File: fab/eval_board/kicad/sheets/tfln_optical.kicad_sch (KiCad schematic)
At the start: 5 parts, among them J11 MPO-24, U21 AD7928, U24 AD5684R, U25 TMP461, U3 TFLN_PIC

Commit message: fix: regenerate KiCad files in valid KiCad 8 format
- Rewrote all .kicad_sch files with proper lib_symbols sections,
  symbol instances, wires, hierarchical sheet references, and
  power port definitions (removed invalid ';;' comment syntax)
- Fixed .kicad_pcb: removed comment lines, added 922 missing net
  definitions, fixed gr_text justify format
- Regenerated Gerbers from fixed PCB using kicad-cli (30 files)
- All files validated with kicad-cli: schematic exports 5-page PDF,
  PCB exports SVG, DRC/ERC both run without parse errors
- Added regenerate_kicad.py generator script for reproducibility

Co-Authored-By: Bola Olatunji <bola.olatunji@ai.lightos.sh>
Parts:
- removed J11: MPO-24, LightRail:MPO-24, symbol Connector:MPO-24
- added J10, J7, J8, J9: SMA_RF_Probe, Connector_Coaxial:SMA_Amphenol_132134-11_Vertical, symbol Connector:SMA
- added J11: MPO-24, LightRail:MPO-24, symbol Connector_Fiber:MPO_24
- U21: value AD7928 -> AD7928BRUZ
- U24: value AD5684R -> AD5684RBRUZ
- U25: value TMP461 -> TMP461AIDR; footprint Package_SON:WSON-8-1EP_2x2mm_P0.5mm -> Package_SO:SOIC-8_3.9x4.9mm_P1.27mm
- U3: value TFLN_PIC -> TFLN_Optical_Module; MPN LR-TFLN-PIC-001 -> (none)
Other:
- note removed: "AC Coupling — TFLN TX Drive: C10_1 through C10_16: 100nF 0201 (GRM033R71A104KA01D) Placed within 1mm of TFLN RF input pads 100Ω differential impedance maintained through coupling"
- note removed: "OPTICAL KEEP-OUT ZONE: 40mm x 15mm centered on TFLN PIC No copper pour, no vias, no traces within ±50µm alignment tolerance Edge-coupler fiber interface at top edge"
- title: TFLN Optical Engine + Monitor/Bias — LightRail Eval Board -> TFLN Optical Engine - LightRail Eval Board

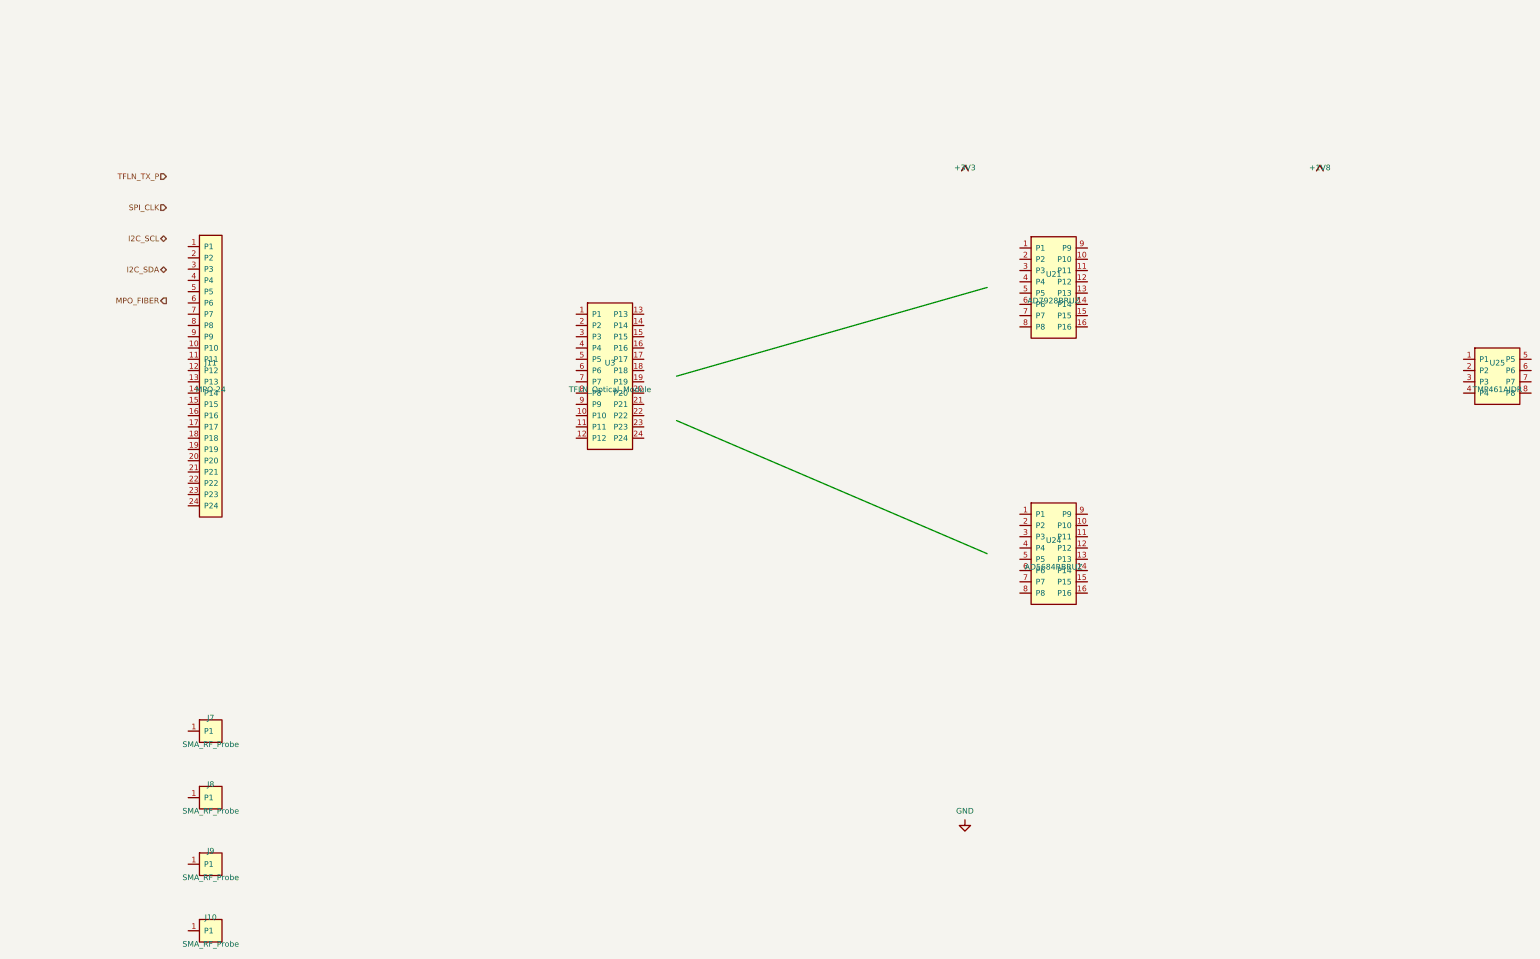
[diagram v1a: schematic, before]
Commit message: refactor: improve ERC quality via grid snapping and power flags
Co-Authored-By: Bola Olatunji <bola.olatunji@ai.lightos.sh>
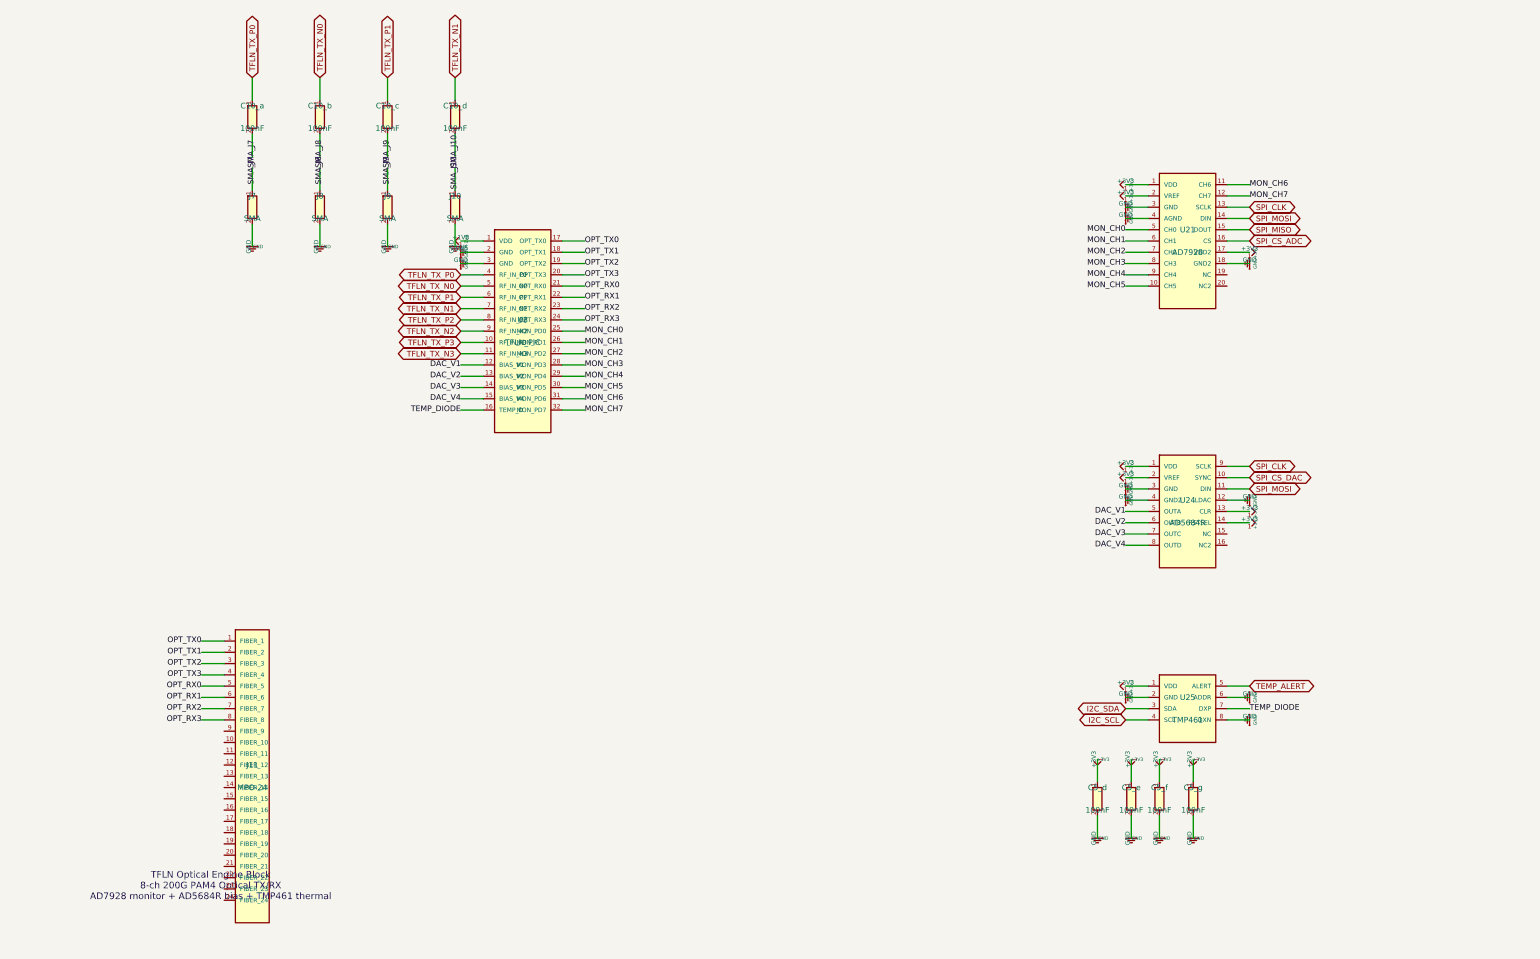
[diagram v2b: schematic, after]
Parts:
- added C10_a, C10_b, C10_c, C10_d, C5_d, C5_e, C5_f, C5_g: 100nF, symbol Device:C
- J10, J7, J8, J9: value SMA_RF_Probe -> SMA; footprint Connector_Coaxial:SMA_Amphenol_132134-11_Vertical -> Connector_Coaxial:SMA_Edge
- J11: footprint LightRail:MPO-24 -> Connector:MPO_24_SMT
- U21: value AD7928BRUZ -> AD7928; footprint Package_SO:TSSOP-20_4.4x6.5mm_P0.65mm -> Package_SO:TSSOP-20
- U24: value AD5684RBRUZ -> AD5684R; footprint Package_SO:TSSOP-16_4.4x5mm_P0.65mm -> Package_SO:TSSOP-16
- U25: value TMP461AIDR -> TMP461; footprint Package_SO:SOIC-8_3.9x4.9mm_P1.27mm -> Package_SON:WSON-8_2x2mm
- U3: value TFLN_Optical_Module -> TFLN_PIC; footprint LightRail:Custom_Optical_Module -> LightRail:TFLN_PIC_Module; MPN (none) -> LR-TFLN-PIC-001
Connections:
- net +1V8: now also U3.1 (VDD)
- net +3V3: now also U21.1 (VDD), U21.17 (VDD2), U21.2 (VREF), U24.1 (VDD), U24.13 (CLR), U24.14 (RSTSEL), U24.2 (VREF), U25.1 (VDD), C5_d.1, C5_e.1, C5_f.1, C5_g.1
- net GND: now also J10.2, J7.2, J8.2, J9.2, U21.18 (GND2), U21.3 (GND), U21.4 (AGND), U24.12 (LDAC), U24.3 (GND), U24.4 (GND2), U25.2 (GND), U25.6 (ADDR), U25.8 (DXN), U3.2 (GND), U3.3 (GND), C5_d.2, C5_e.2, C5_f.2, C5_g.2
- net I2C_SCL: now also U25.4 (SCL)
- net I2C_SDA: now also U25.3 (SDA)
- net SPI_CLK: now also U21.13 (SCLK), U24.9 (SCLK)
- net SMA_J10: now reaches J10.1
- net SMA_J10: now also C10_d.2
- net SMA_J8: now reaches J8.1
- net SMA_J8: now also C10_b.2
- net OPT_TX0: now reaches J11.1 (FIBER_1)
- net OPT_TX0: now also U3.17 (OPT_TX0)
- net OPT_TX1: now reaches J11.2 (FIBER_2)
- net OPT_TX1: now also U3.18 (OPT_TX1)
- net OPT_TX2: now reaches J11.3 (FIBER_3)
- net OPT_TX2: now also U3.19 (OPT_TX2)
- net OPT_TX3: now reaches J11.4 (FIBER_4)
- net OPT_TX3: now also U3.20 (OPT_TX3)
- net OPT_RX0: now reaches J11.5 (FIBER_5)
- net OPT_RX0: now also U3.21 (OPT_RX0)
- net OPT_RX1: now reaches J11.6 (FIBER_6)
- net OPT_RX1: now also U3.22 (OPT_RX1)
- net OPT_RX2: now reaches J11.7 (FIBER_7)
- net OPT_RX2: now also U3.23 (OPT_RX2)
- net OPT_RX3: now reaches J11.8 (FIBER_8)
- net OPT_RX3: now also U3.24 (OPT_RX3)
- net MON_CH5: now reaches U21.10 (CH5)
- net MON_CH5: now also U3.30 (MON_PD5)
- net MON_CH6: now reaches U21.11 (CH6)
- net MON_CH6: now also U3.31 (MON_PD6)
- net MON_CH7: now reaches U21.12 (CH7)
- net MON_CH7: now also U3.32 (MON_PD7)
- net SPI_MOSI: now reaches U21.14 (DIN)
- net SPI_MOSI: now also U24.11 (DIN)
- net SPI_MISO: now reaches U21.15 (DOUT)
- net SPI_CS_ADC: now reaches U21.16 (CS)
- net MON_CH0: now reaches U21.5 (CH0)
- net MON_CH0: now also U3.25 (MON_PD0)
- net MON_CH1: now reaches U21.6 (CH1)
- net MON_CH1: now also U3.26 (MON_PD1)
- net MON_CH2: now reaches U21.7 (CH2)
- net MON_CH2: now also U3.27 (MON_PD2)
- net MON_CH3: now reaches U21.8 (CH3)
- net MON_CH3: now also U3.28 (MON_PD3)
- net MON_CH4: now reaches U21.9 (CH4)
- net MON_CH4: now also U3.29 (MON_PD4)
- net TEMP_ALERT: now reaches U25.5 (ALERT)
- net TEMP_DIODE: now reaches U25.7 (DXP)
- net TEMP_DIODE: now also U3.16 (TEMP_D)
- net SPI_CS_DAC: now reaches U24.10 (SYNC)
- net DAC_V1: now reaches U24.5 (OUTA)
- net DAC_V1: now also U3.12 (BIAS_V1)
- net DAC_V2: now reaches U24.6 (OUTB)
- net DAC_V2: now also U3.13 (BIAS_V2)
- net DAC_V3: now reaches U24.7 (OUTC)
- net DAC_V3: now also U3.14 (BIAS_V3)
- net DAC_V4: now reaches U24.8 (OUTD)
- net DAC_V4: now also U3.15 (BIAS_V4)
- net SMA_J7: now reaches J7.1
- net SMA_J7: now also C10_a.2
- net TFLN_TX_P3: now reaches U3.10 (RF_IN_P3)
- net TFLN_TX_N3: now reaches U3.11 (RF_IN_N3)
- net TFLN_TX_P0: now reaches U3.4 (RF_IN_P0)
- net TFLN_TX_P0: now also C10_a.1
- net TFLN_TX_N0: now reaches U3.5 (RF_IN_N0)
- net TFLN_TX_N0: now also C10_b.1
- net TFLN_TX_P1: now reaches U3.6 (RF_IN_P1)
- net TFLN_TX_P1: now also C10_c.1
- net TFLN_TX_N1: now reaches U3.7 (RF_IN_N1)
- net TFLN_TX_N1: now also C10_d.1
- net TFLN_TX_P2: now reaches U3.8 (RF_IN_P2)
- net TFLN_TX_N2: now reaches U3.9 (RF_IN_N2)
- net SMA_J9: now reaches J9.1
- net SMA_J9: now also C10_c.2
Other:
- note added: "TFLN Optical Engine Block 8-ch 200G PAM4 Optical TX/RX AD7928 monitor + AD5684R bias + TMP461 thermal"
- title: TFLN Optical Engine - LightRail Eval Board -> TFLN Optical - LightRail Eval Board
